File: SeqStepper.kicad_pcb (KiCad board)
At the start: 2 copper layers, 28.5 x 13.5 mm, 3 parts, among them J1 In, J2 ST1, J3 ST2

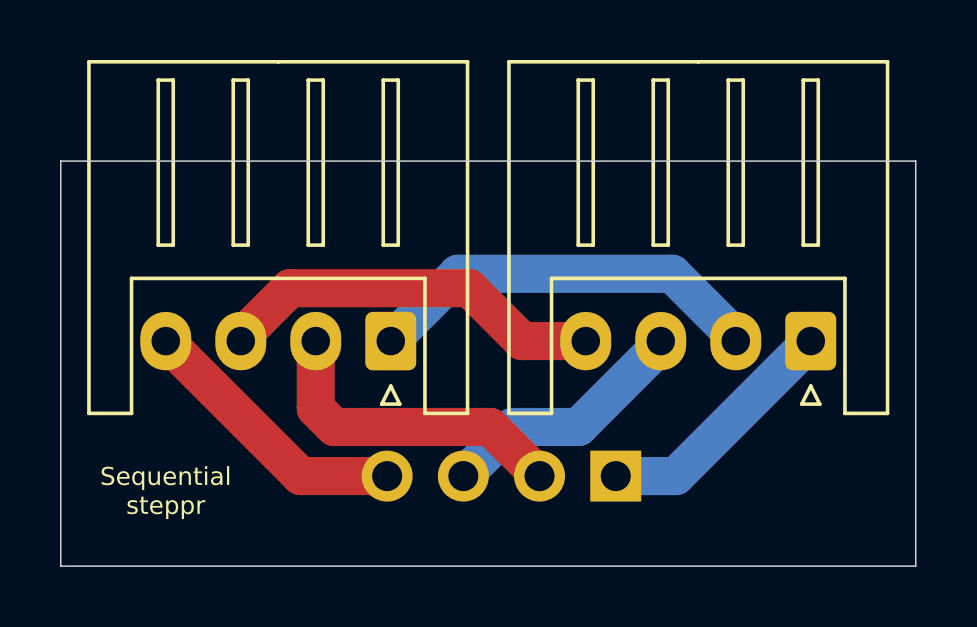
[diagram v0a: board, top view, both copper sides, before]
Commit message: Update traces with more copper.
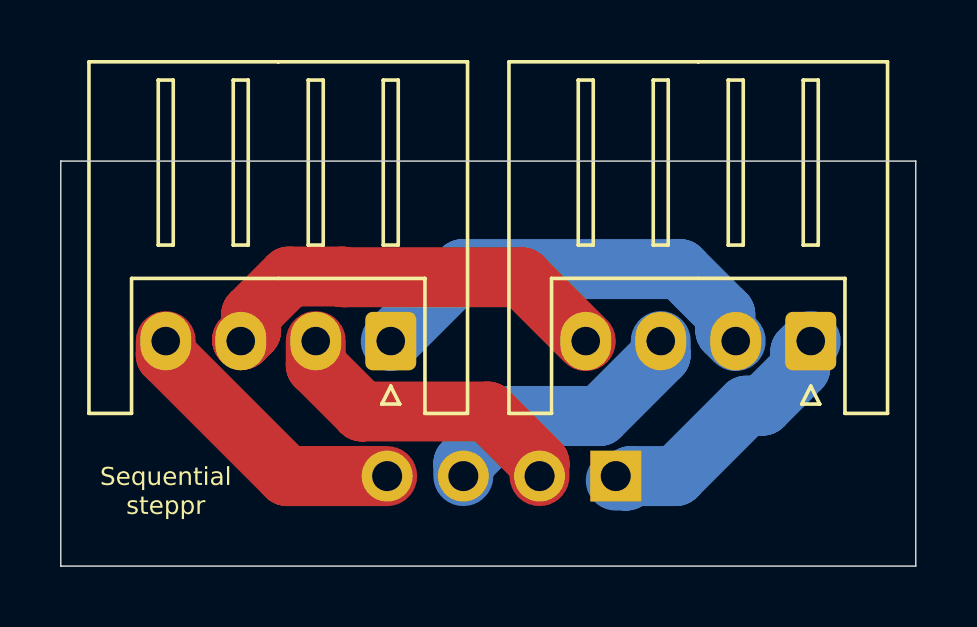
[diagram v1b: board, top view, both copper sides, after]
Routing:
- net Net-(J2-Pad4): track 13.0 -> 13.7 mm
- net Net-(J1-Pad2): track 10.6 -> 10.0 mm
- net Net-(J1-Pad3): track 8.52 -> 9.08 mm
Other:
- net class Default removed
- board text added: "(c) iQury.us Jan 2021"
- board text removed: "(c) iQury.us Nov 2019"
